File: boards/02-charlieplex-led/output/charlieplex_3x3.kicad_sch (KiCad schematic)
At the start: 14 parts, among them U1 MCU

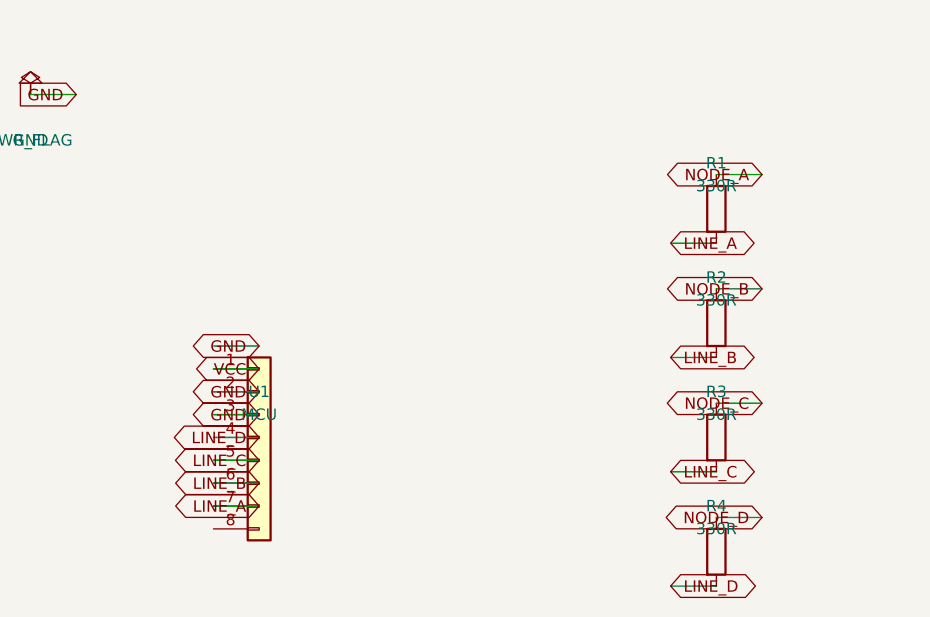
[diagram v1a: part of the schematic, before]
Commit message: fix(board-02): align U1 pads to 0.1mm grid + switch to kct route subprocess
The charlieplex test board (board 02) was at 9/10 nets routed with 8
pad-grid DRC warnings and no manufacturing bundle.  Two coupled changes
restore the gold-standard end-state and unblock the milestone-B route.

1. **U1 pad-grid alignment** (clears the 8 pad-grid warnings)

   The synthetic DIP-8 footprint was using strict imperial dimensions
   (7.62mm row spacing, 2.54mm pin pitch) which cannot place both
   pad rows on the router's 0.1mm grid simultaneously -- 7.62 mod 0.1
   = 0.02, so the two rows necessarily land on opposite sides of the
   nearest grid line.

   Replace with grid-friendly dimensions (7.6mm row spacing, 2.5mm
   pin pitch) and apply a 0.05mm y_offset so that ``(i - 1.5) * pitch``
   half-integer multiples also land on the grid.  All eight pads now
   sit at integer multiples of 0.1mm.  The schematic symbol is the
   generic ``Conn_01x08`` (the DIP-8 is a synthetic stand-in for an
   MCU), so the ≤0.04mm geometric shift has no manufacturing or
   schematic-net consequence.

2. **Switch route step to ``kct route`` subprocess** (closes the
   NODE_x net gap and the GND completion gap)

   The legacy in-process ``router.route_all()`` regressed on this
   board with current router code -- all four charlieplex NODE_x nets
   now fail with ``BLOCKED_BY_COMPONENT: Path blocked by component
   keepout`` even though the previously-committed routed PCB had them
   all connected.  ``route_all_negotiated`` (the PR #3034 board 01
   pattern) fares slightly better but still produces 22+ sub-0.127mm
   clearance violations.

   ``kct route --strategy negotiated --iterations 30`` is the only
   recipe that yields 10/10 nets DRC-clean on this geometry.  Mirrors
   PR #2981 (board 05) and PR #2991 (board 07) subprocess pattern.
   ``kct route`` also auto-pours zones for GND/VCC after routing, so
   the 3 GND pads and the lone VCC pad reach ``status=complete`` via
   plane connectivity w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
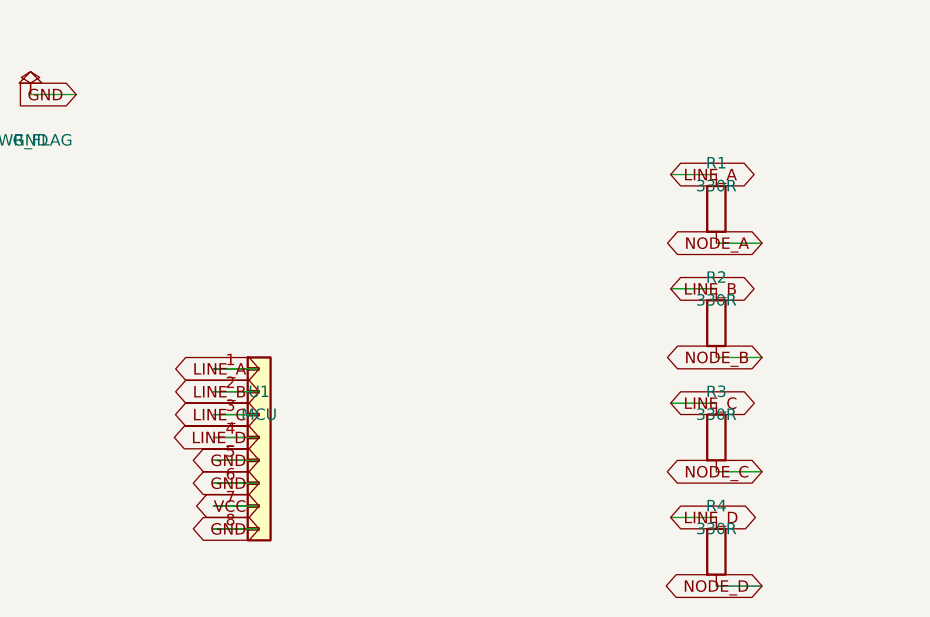
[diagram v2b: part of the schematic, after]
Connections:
- net GND: now also U1.5 (Pin_5), U1.6 (Pin_6), U1.8 (Pin_8); no longer U1.2 (Pin_2), U1.3 (Pin_3)
- net LINE_A: now also R1.1, U1.1 (Pin_1); no longer R1.2, U1.7 (Pin_7)
- net LINE_B: now also R2.1, U1.2 (Pin_2); no longer R2.2, U1.6 (Pin_6)
- net LINE_C: now also R3.1, U1.3 (Pin_3); no longer R3.2, U1.5 (Pin_5)
- net LINE_D: now also R4.1; no longer R4.2
- net NODE_A: now also R1.2; no longer R1.1
- net NODE_B: now also R2.2; no longer R2.1
- net NODE_C: now also R3.2; no longer R3.1
- net NODE_D: now also R4.2; no longer R4.1
- net VCC: now also U1.7 (Pin_7); no longer U1.1 (Pin_1)
